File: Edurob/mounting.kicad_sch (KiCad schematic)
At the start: 42 parts

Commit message: Finished routing and part placement
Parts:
- removed H13, H14, H25, H26, H27, H28, H37, H42: 9775026360R, Footprints:9775026360R, symbol 9775026360R:9775026360R

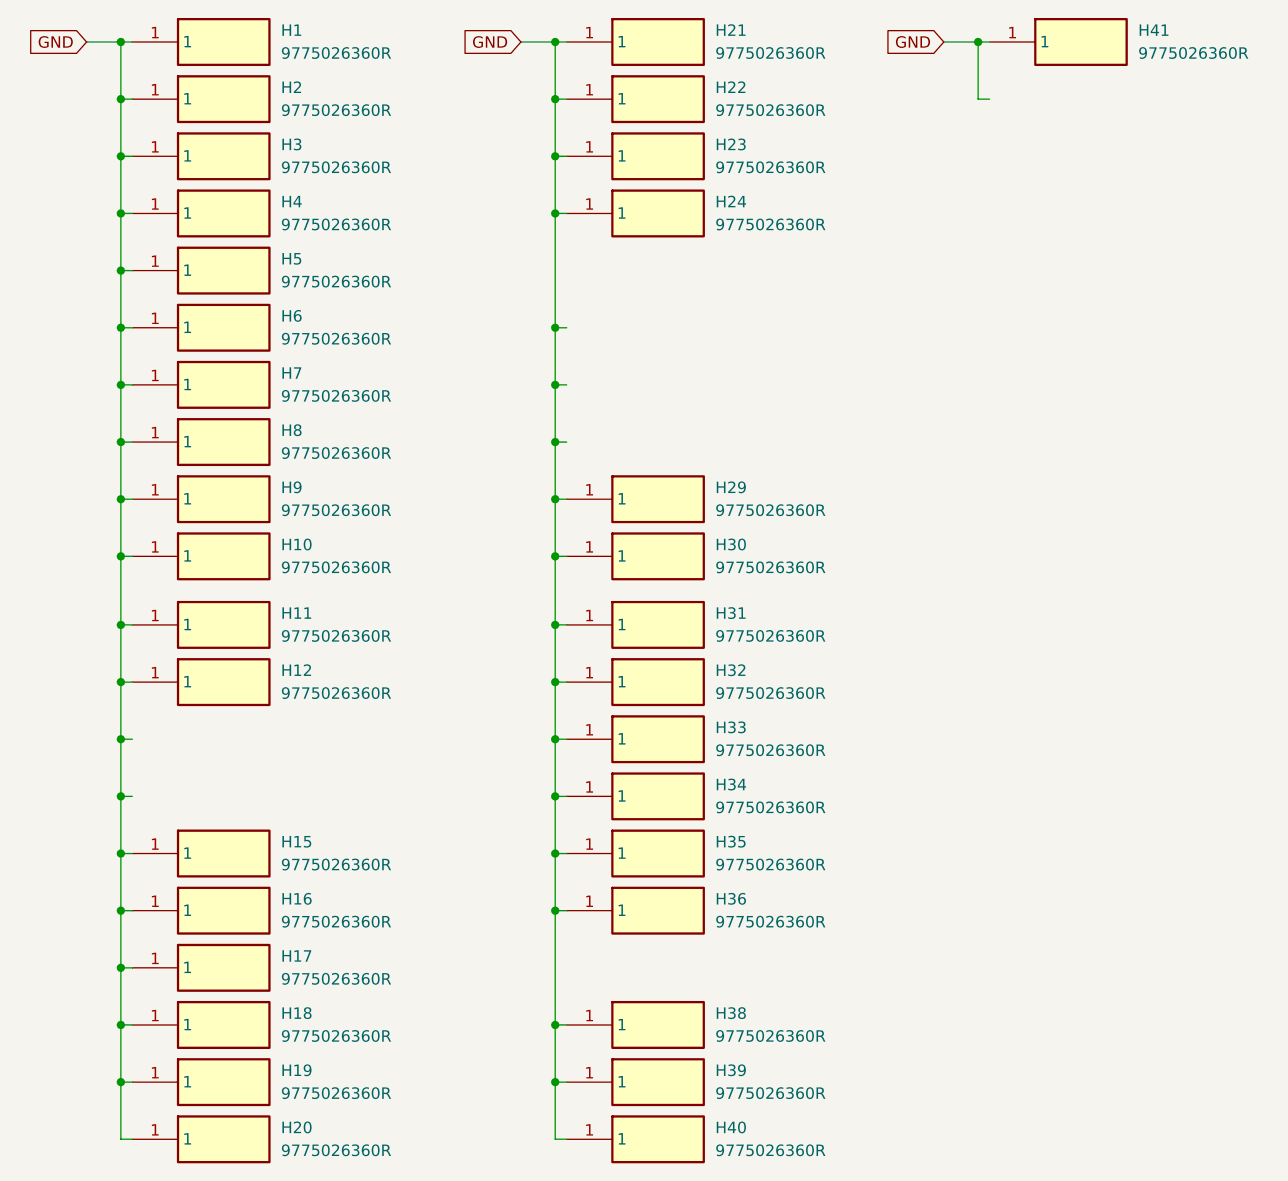
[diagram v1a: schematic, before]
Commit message: Finished silkscreen + fixed board outline
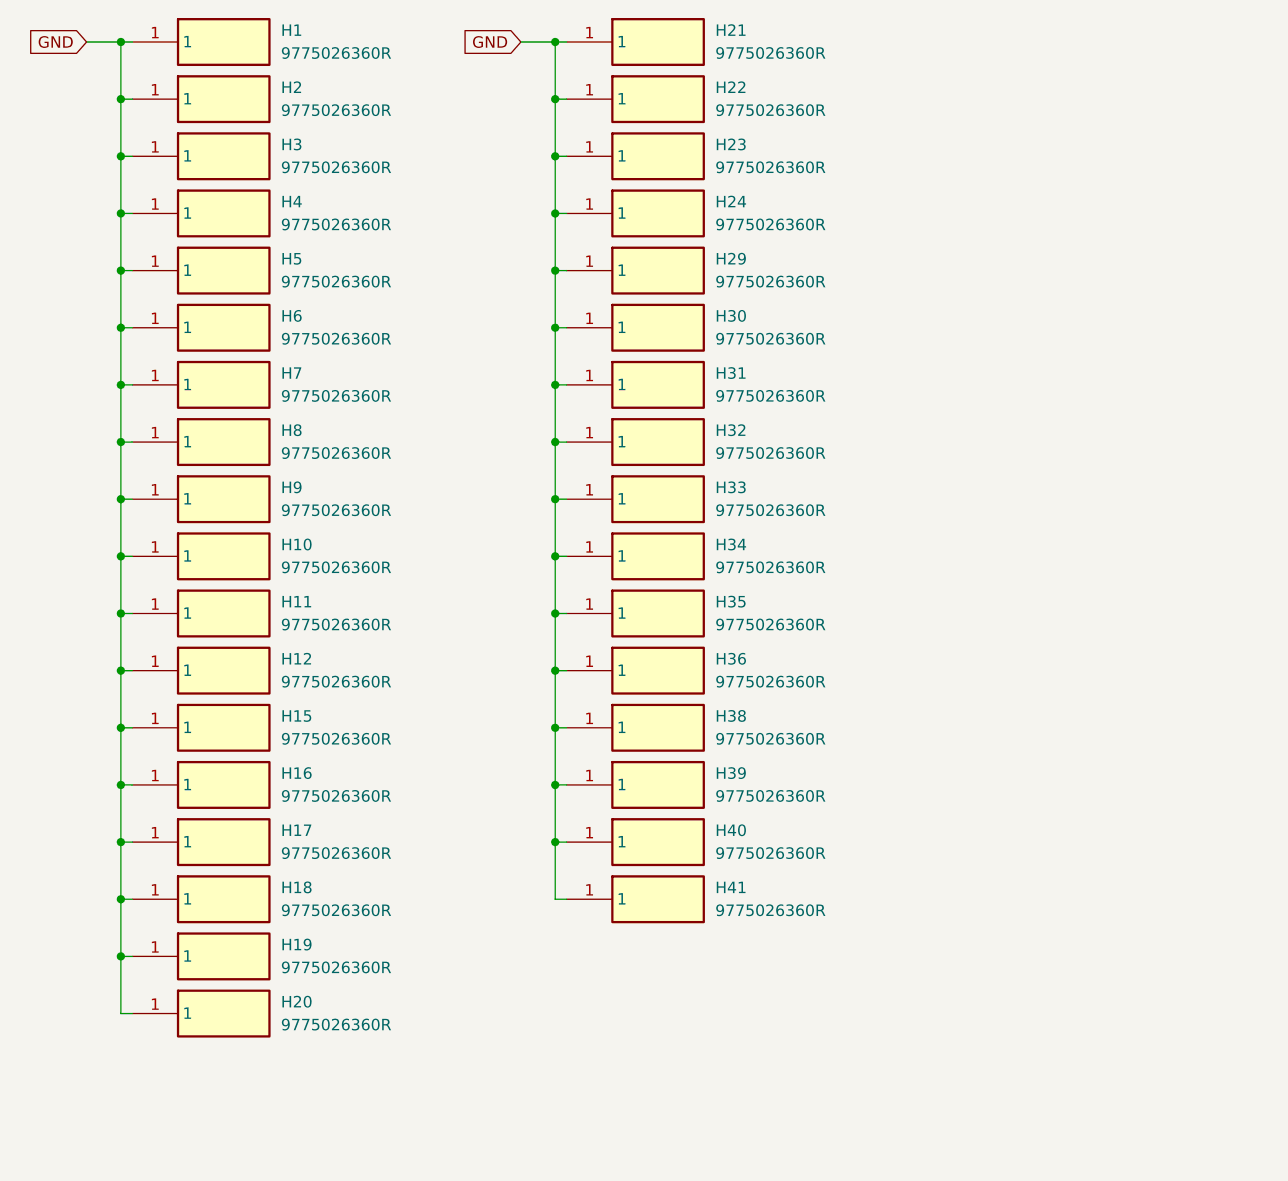
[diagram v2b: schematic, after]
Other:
- moved on the sheet: H11, H12, H15, H16, H17, H18, H19, H20, H29, H30, H31, H32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

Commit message: Release v1.0.1
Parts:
- H1, H10, H11, H12, H15, H16, H17, H18, H19, H2, H20, H21, H22, H23, H24, H29, H3, H30, H31, H32, H33, H34, H35, H36, H38, H39, H4, H40, H41, H5, H6, H7, H8, H9: value 9775026360R -> SMTSO-M3-2ET; footprint Footprints:9775026360R -> Footprints:SMTSO-M3-2ET; Height 1 -> (none); Manufacturer_Name Wurth Elektronik -> PEM; Manufacturer_Part_Number 9775026360R -> SMTSO-M3-2ET; Mouser Part Number 710-9775026360R -> 153-SMTSO-M3-2ET; Mouser Price/Stock https://www.mouser.co.uk/ProductDetail/Wurth-Elektronik/977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 -> https://www.mouser.de/ProductDetail/153-SMTSO-M3-2ET; Placed (none) -> True
